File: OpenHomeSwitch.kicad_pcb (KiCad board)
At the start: 4 copper layers, 82.5 x 65.5 mm, 283 parts, among them J10 USB_C_Receptacle_USB2.0, J11 USB_C_Receptacle_USB2.0, J2 Conn_01x04, J3 Conn_01x04, J4 Micro_SD_Card_Det2, J5 Conn_01x04, J6 Extension I2C, J7 Conn_01x04, J8 Debug, J9 Extension UART, Q1 2N7002, Q10 MMBT3904, Q2 MMBT3904, Q3 MMBT3904, Q4 MMBT5401, Q5 AO3401A, Q6 MMBT5401, Q7 MMBT5401, Q8 AO3401A, Q9 MMBT5401, U1 RTL8367RB, U2 Allwinner_V3S, U3 TMI7003x, U4 TMI7003x, U5 W25Q128JVS, U6 SRV05-4, Y1 25MHz, Y2 24MHz, Y3 32.768kHz

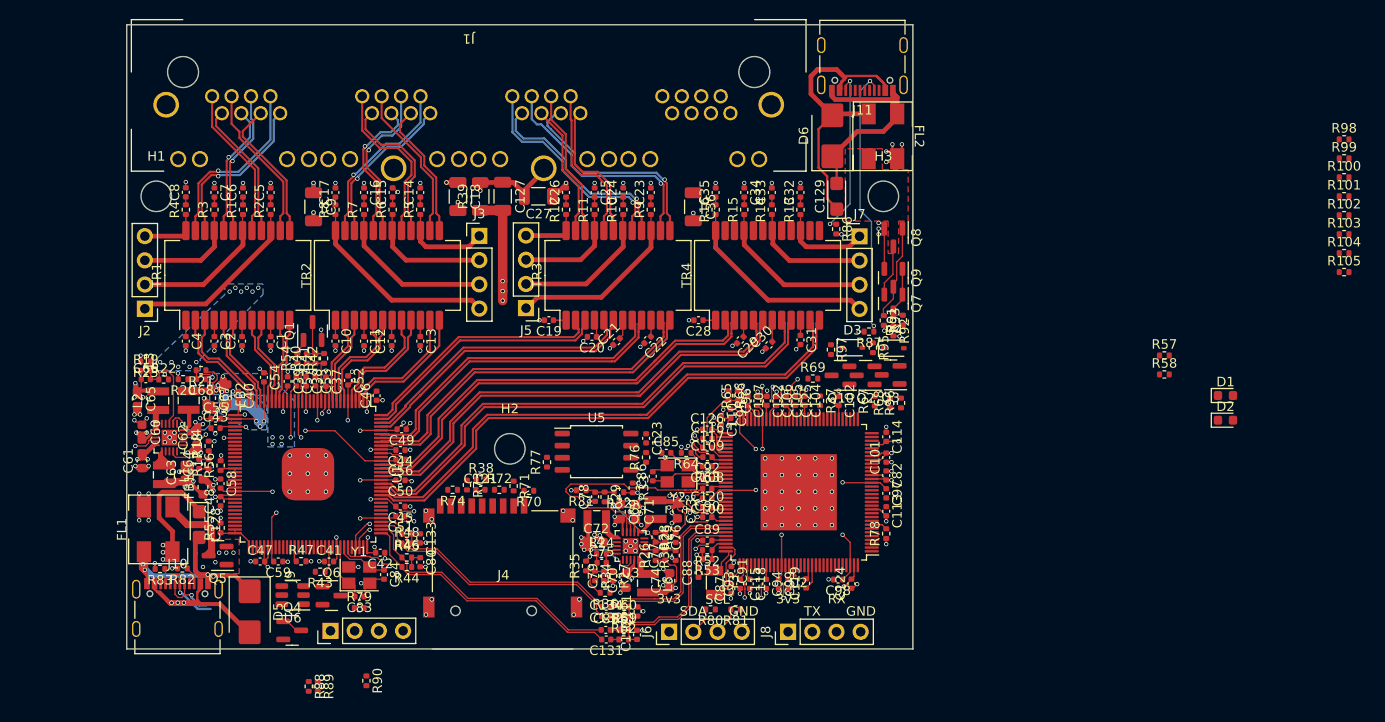
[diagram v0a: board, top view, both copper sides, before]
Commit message: Finish routing for the most part
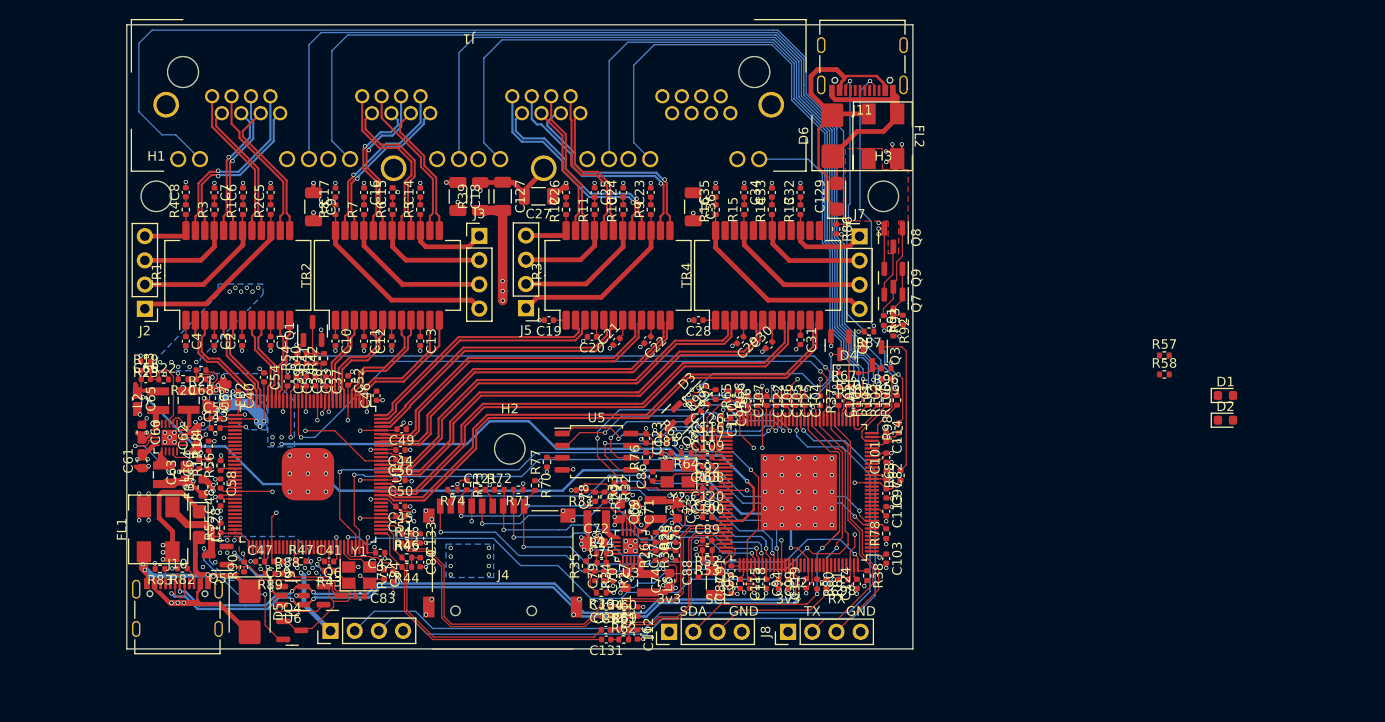
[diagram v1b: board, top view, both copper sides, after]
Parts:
- added C103: 1nF, Capacitor_SMD:C_0402_1005Metric, F.Cu at (223.2, 119.5)
- moved R98 55.7 mm to (224.5, 105.8), turned to 90 degrees
- moved R104 53.9 mm to (219.8, 103.3)
- moved R101 53.4 mm to (222.3, 102.9), turned to 90 degrees
- moved R99 53.3 mm to (223.3, 100.7), turned to 180 degrees
- moved R105 53.2 mm to (219.7, 102.5)
- moved R103 53.0 mm to (221.2, 102.9), turned to 90 degrees
- moved R100 52.4 mm to (224.3, 102.9), turned to 90 degrees
- moved R102 51.8 mm to (223.2, 102.9), turned to 90 degrees
- moved R38 41.8 mm to (221.2, 121.3), turned to -90 degrees
- moved Q10 17.8 mm to (201.2, 104.9), turned to -135 degrees
- moved R90 17.5 mm to (155.8, 120.4), turned to 90 degrees
- moved R95 17.2 mm to (205.3, 102.3), turned to 90 degrees
- moved R69 16.9 mm to (199.8, 107.0), turned to -45 degrees
- moved D3 16.8 mm to (203.6, 102.2), turned to 45 degrees
- moved R97 14.6 mm to (204.2, 103.7), turned to 45 degrees
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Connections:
- J8 pad 2: /CPU/DEBUG_TX -> /CPU/DEBUG_RX
- J8 pad 3: /CPU/DEBUG_RX -> /CPU/DEBUG_TX
- J9 pad 2: /CPU/UART0_TX -> /CPU/UART0_RX
- J9 pad 3: /CPU/UART0_RX -> /CPU/UART0_TX
- R100 pad 1: /CPU/SWITCH_LED_P3_YLW -> /CPU/SWITCH_LED_P4_YLW
- R100 pad 2: Net-(J1-Pad22) -> Net-(J1-Pad10)
- R101 pad 1: /CPU/SWITCH_LED_P3_GRN -> /CPU/SWITCH_LED_P2_GRN
- R101 pad 2: Net-(J1-Pad24) -> Net-(J1-Pad36)
- R102 pad 1: /CPU/SWITCH_LED_P2_YLW -> /CPU/SWITCH_LED_P3_YLW
- R102 pad 2: Net-(J1-Pad34) -> Net-(J1-Pad22)
- R103 pad 1: /CPU/SWITCH_LED_P2_GRN -> /CPU/SWITCH_LED_P2_YLW
- R103 pad 2: Net-(J1-Pad36) -> Net-(J1-Pad34)
- R104 pad 1: /CPU/SWITCH_LED_P1_YLW -> /CPU/SWITCH_LED_P1_GRN
- R104 pad 2: Net-(J1-Pad46) -> Net-(J1-Pad48)
- R105 pad 1: /CPU/SWITCH_LED_P1_GRN -> /CPU/SWITCH_LED_P1_YLW
- R105 pad 2: Net-(J1-Pad48) -> Net-(J1-Pad46)
- R99 pad 1: /CPU/SWITCH_LED_P4_YLW -> /CPU/SWITCH_LED_P3_GRN
- R99 pad 2: Net-(J1-Pad10) -> Net-(J1-Pad24)
- U2 pad 100: unconnected-(U2G-PF6-Pad100) -> /CPU/SWITCH_~{RST}
- U2 pad 23: /CPU/SWITCH_LED_P4_YLW -> unconnected-(U2F-PE11/CSI_D7/LCD_D11-Pad23)
- U2 pad 24: /CPU/SWITCH_LED_P4_GRN -> unconnected-(U2F-PE10/CSI_D6/LCD_D10-Pad24)
- U2 pad 30: unconnected-(U2F-PE7/CSI_D3/LCD_D5-Pad30) -> /CPU/SWITCH_LED_P3_GRN
- U2 pad 31: /CPU/SWITCH_LED_P3_YLW -> /CPU/SWITCH_LED_P4_GRN
- U2 pad 32: /CPU/SWITCH_LED_P3_GRN -> /CPU/SWITCH_LED_P4_YLW
- U2 pad 33: /CPU/SWITCH_LED_P2_YLW -> /CPU/SWITCH_LED_P2_GRN
- U2 pad 34: /CPU/SWITCH_LED_P2_GRN -> /CPU/SWITCH_LED_P3_YLW
- U2 pad 35: /CPU/SWITCH_LED_P1_YLW -> /CPU/SWITCH_LED_P2_YLW
- U2 pad 37: /CPU/SWITCH_~{RST} -> /CPU/SWITCH_LED_P1_YLW
- U6 pad 1: /USB_D- -> /USB_D+
- U6 pad 3: /USB_D+ -> /USB_D-
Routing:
- net Net-(J1-Pad12): track 0.00 -> 130.2 mm, vias 0 -> 1
- net Net-(J1-Pad10): track 0.00 -> 105.0 mm, vias 0 -> 1
- net Net-(J1-Pad24): track 0.00 -> 101.7 mm, vias 0 -> 1
- net Net-(J1-Pad22): track 0.00 -> 88.2 mm, vias 0 -> 1
- net Net-(J1-Pad36): track 0.00 -> 84.8 mm, vias 0 -> 1
- net /CPU/UART0_RX: track 0.00 -> 80.7 mm, vias 0 -> 1
- net +3V0: track 41.2 -> 120.9 mm
- net /CPU/UART0_TX: track 0.00 -> 78.7 mm, vias 0 -> 1
- net /USB_D+: track 8.06 -> 77.7 mm, vias 1 -> 4
- net Net-(J1-Pad34): track 0.00 -> 69.4 mm, vias 0 -> 1
- net Net-(J1-Pad48): track 0.00 -> 67.8 mm, vias 0 -> 1
- net /USB_D-: track 9.18 -> 75.6 mm, vias 1 -> 4
- net /CPU/MDC: track 3.22 -> 68.9 mm, vias 1 -> 2
- net /CPU/SWITCH_IRQ: track 3.92 -> 67.6 mm, vias 1 -> 2
- net /CPU/MDIO: track 4.09 -> 67.6 mm, vias 1 -> 2
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
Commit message: Finish signal routing
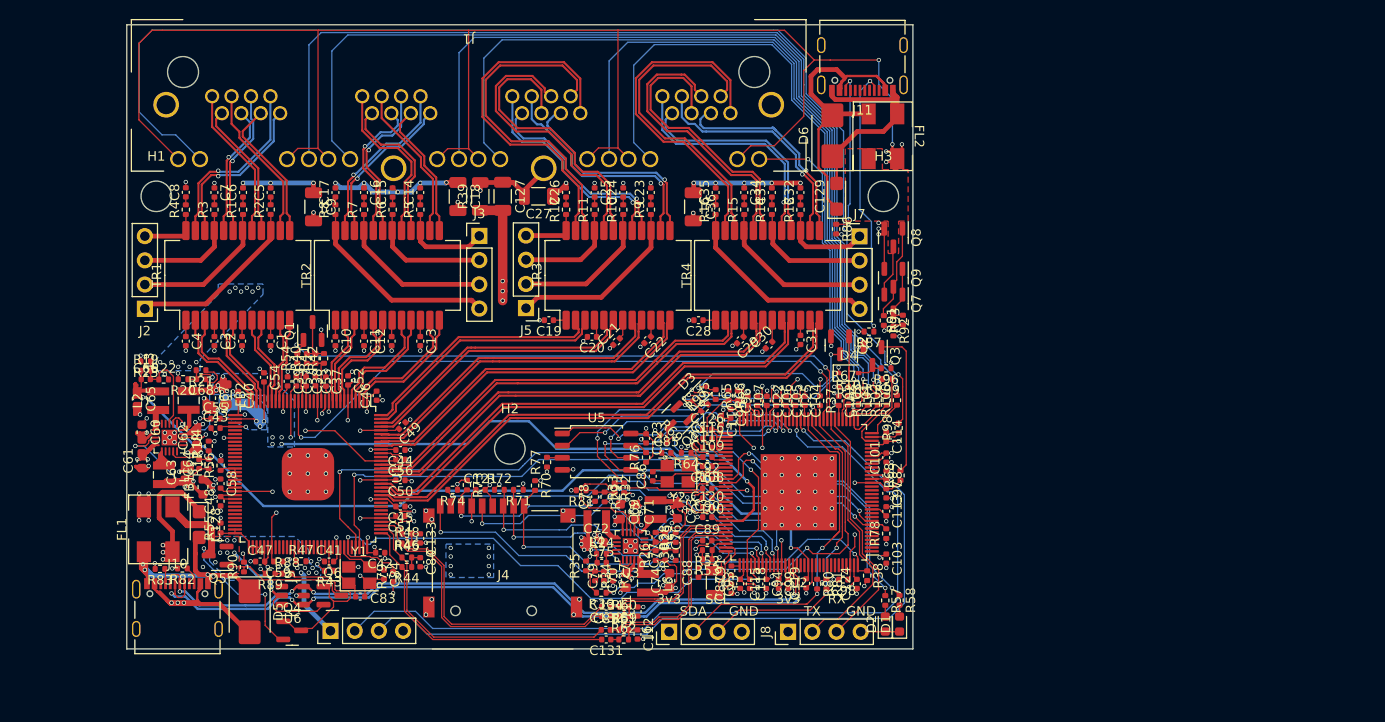
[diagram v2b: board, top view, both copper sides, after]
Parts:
- moved D1 41.8 mm to (224.6, 126.4), turned to 90 degrees
- moved D2 41.6 mm to (223.1, 126.4), turned to 90 degrees
- moved R57 39.0 mm to (223.1, 123.9), turned to -90 degrees
- moved R58 36.5 mm to (224.6, 123.9), turned to -90 degrees
- moved C49 0.39 mm to (172.4, 105.6), turned to -135 degrees
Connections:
- J1 pad 28: /Switch/Switch ports/P2DM- -> /Switch/Switch ports/P2CM+
- J1 pad 29: /Switch/Switch ports/P2DM+ -> /Switch/Switch ports/P2CM-
- J1 pad 31: /Switch/Switch ports/P2CM- -> /Switch/Switch ports/P2DM+
- J1 pad 32: /Switch/Switch ports/P2CM+ -> /Switch/Switch ports/P2DM-
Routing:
- net GND: track 194.6 -> 369.7 mm, vias 205 -> 206
- net /Switch/Switch ports/P1DM-: track 0.00 -> 36.2 mm
- net /Switch/Switch ports/P1DM+: track 0.00 -> 33.6 mm
- net /Switch/Switch ports/P1CM+: track 0.00 -> 30.4 mm
- net /Switch/Switch ports/P1CM-: track 0.00 -> 30.0 mm
- net Net-(U2I-EPHY_LINK_LED): track 0.00 -> 30.0 mm, vias 0 -> 2
- net Net-(U2I-EPHY_SPD_LED): track 0.00 -> 28.6 mm, vias 0 -> 2
- net /Switch/Switch ports/P1BM-: track 0.00 -> 25.1 mm, vias 0 -> 1
- net /Switch/Switch ports/P1AM-: track 0.00 -> 24.7 mm, vias 0 -> 1
- net /Switch/Switch ports/P2DM-: track 14.0 -> 37.9 mm
- net /Switch/Switch ports/P1BM+: track 0.00 -> 23.6 mm, vias 0 -> 1
- net /Switch/Switch ports/P1AM+: track 0.00 -> 22.9 mm, vias 0 -> 1
- net /Switch/Switch ports/P2DM+: track 15.6 -> 35.2 mm
- net /Switch/Switch ports/P2CM+: track 15.2 -> 30.8 mm
- net /Switch/Switch ports/P2CM-: track 16.7 -> 30.3 mm
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
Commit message: Finalize design
- Layout last signals
- Hide designators
- Add more LEDs
- Add tooling holes
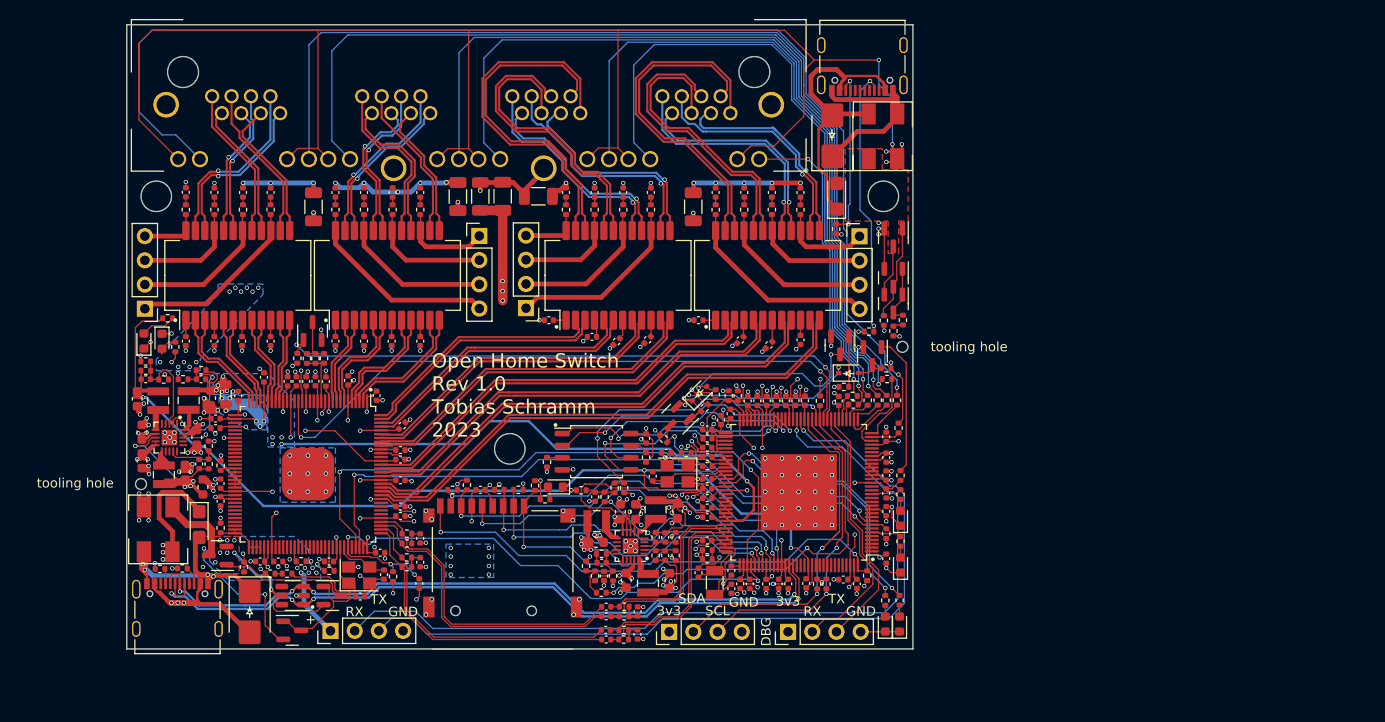
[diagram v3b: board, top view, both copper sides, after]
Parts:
- added C130: 1nF, Capacitor_SMD:C_0402_1005Metric, F.Cu at (174.2, 122.1)
- added D10: RED, LED_SMD:LED_0603_1608Metric, F.Cu at (224.7, 115.3)
- added D12: GRN, LED_SMD:LED_0603_1608Metric, F.Cu at (224.7, 120.2)
- added D7: RED, LED_SMD:LED_0603_1608Metric, F.Cu at (147.2, 96.7)
- added D8: WHT, LED_SMD:LED_0603_1608Metric, F.Cu at (145.3, 96.7)
- added D9: GRN, LED_SMD:LED_0603_1608Metric, F.Cu at (188.5, 112.0)
- added H4: ToolingHole, ToolingHole:ToolingHole_JLCSMT, F.Cu at (224.9, 97.3)
- added H5: ToolingHole, ToolingHole:ToolingHole_JLCSMT, F.Cu at (145.0, 111.7)
- added R49: 6.8k, Resistor_SMD:R_0402_1005Metric, F.Cu at (148.6, 97.3)
- added R50: 6.8k, Resistor_SMD:R_0402_1005Metric, F.Cu at (147.8, 94.3)
- added R51: 6.8k, Resistor_SMD:R_0402_1005Metric, F.Cu at (187.4, 113.3)
- added R75: 2.2k, Resistor_SMD:R_0402_1005Metric, F.Cu at (224.7, 112.8)
- added R85: 6.8k, Resistor_SMD:R_0402_1005Metric, F.Cu at (224.7, 117.7)
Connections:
- U2 pad 16: unconnected-(U2F-PE15/CSI_D11/LCD_D15-Pad16) -> Net-(U2F-PE15/CSI_D11/LCD_D15)
- U2 pad 6: unconnected-(U2F-PE24/LCD_D23/UART1_CTS-Pad6) -> Net-(U2F-PE24/LCD_D23/UART1_CTS)
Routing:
- net GND: track 369.7 -> 378.8 mm, vias 206 -> 212
- net +3V0: track 122.2 -> 129.7 mm
- net /CPU/SWITCH_~{RST}: track 56.6 -> 60.3 mm, vias 2 -> 4
- net Net-(D8-A): track 0.00 -> 3.66 mm
- net Net-(U2F-PE24/LCD_D23/UART1_CTS): track 0.00 -> 3.27 mm
- net Net-(U2F-PE15/CSI_D11/LCD_D15): track 0.00 -> 3.21 mm
- net +3V3: track 109.4 -> 111.4 mm
- net Net-(D7-A): track 0.00 -> 1.69 mm
- net Net-(D9-A): track 0.00 -> 1.40 mm
- net Net-(D10-A): track 0.00 -> 1.30 mm
- net Net-(D12-A): track 0.00 -> 1.21 mm
- net VBUS: track 89.1 -> 88.0 mm, vias 51 -> 52
- net Net-(Q3-B): track 15.4 -> 14.7 mm
- added copper zone on B.Cu, net GND
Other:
- board text added: "+"
- board text added: "DBG"
- board text added: "Open Home Switch Rev 1.0 Tobias Schramm 2023"
